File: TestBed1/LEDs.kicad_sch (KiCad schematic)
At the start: 6 parts, among them U3 TLC5973

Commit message: WIP - Parts Assigned
Need footprints, and MCU connections, but WIP
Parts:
- removed D1, D2, D3: D, symbol Device:D
- added C10, C8: 0.1u, symbol Device:C
- added C11: C, symbol Device:C
- added D1, D2, D3: LED, LED_SMD:LED_1206_3216Metric, symbol Device:LED
- added R5: 0, symbol Device:R
- added U6: TXB0101DBV, Package_TO_SOT_SMD:SOT-23-6, symbol Logic_LevelTranslator:TXB0101DBV
- added U7: ~, symbol New_Library:SFH_5711-2/3-Z
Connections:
- net +3V3: now also C11.1, C8.1, R5.1, U6.1 (V_{CCA}), U7.3 (VCC); no longer C2.1, U3.8 (VCC)
- net D1: now also D1.1 (K), D2.1 (K), D3.1 (K)
- net GND: now also C10.2, C11.2, C8.2, U6.2 (GND), U7.1 (GND), U7.2 (GND)
- net LED_IN: now also U6.3 (A); no longer U3.6 (SDI)
- new net: R5.2, U6.5 (OE)
- new net +5V: C10.1, C2.1, D1.2 (A), D2.2 (A), D3.2 (A), U3.8 (VCC), U6.6 (V_{CCB})
- new net AMB_OUT: U7.4 (OUT)
- new net LED_OUT: U3.6 (SDI), U6.4 (B)
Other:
- note added: "TODO BH1620FVC-TR Ambient"
- note removed: "TODO BH1620FVC"

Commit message: LED Update for more work
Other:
- note added: "TODO Heartbeat LED"
- note added: "TODO MCU crashed LED"
- note added: "TODO maybe intend to extend further with more of above LED drivers?"
- note added: "TODO reserve castelated area?"
- note added: "TODO reverse mounted warning indicators."
- note added: "TODO swap whites for reds"
- moved on the sheet: C11, U7
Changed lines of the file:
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@@
 	(paper "A4")
 	(junction
-		(at 121.92 149.86)
+		(at 146.05 175.26)
 		(diameter 0)
 		(color 0 0 0 0)
@@
 	(wire
 		(pts
-			(xy 123.19 149.86) (xy 123.19 148.59)
+			(xy 147.32 175.26) (xy 147.32 173.99)
 		)
 		(stroke
@@
 	(wire
 		(pts
-			(xy 121.92 151.13) (xy 121.92 149.86)
+			(xy 146.05 176.53) (xy 146.05 175.26)
 		)
 		(stroke
@@
 	(wire
 		(pts
-			(xy 121.92 149.86) (xy 120.65 149.86)
+			(xy 146.05 175.26) (xy 144.78 175.26)
 		)
 		(stroke
@@
 	(wire
 		(pts
-			(xy 121.92 149.86) (xy 123.19 149.86)
+			(xy 146.05 175.26) (xy 147.32 175.26)
 		)
 		(stroke
@@
 	(wire
 		(pts
-			(xy 120.65 149.86) (xy 120.65 148.59)
+			(xy 144.78 175.26) (xy 144.78 173.99)
 		)
 		(stroke
@@
 		)
 	)
+	(text "TODO swap whites for reds"
+		(exclude_from_sim no)
+		(at 110.744 89.408 0)
+		(effects
+			(font
+				(size 1.27 1.27)
+			)
+		)
+	)
+	(text "TODO maybe intend to extend further with more of above LED drivers?"
+		(exclude_from_sim no)
+		(at 143.764 115.824 0)
+		(effects
+			(font
+				(size 1.27 1.27)
+			)
+		)
+	)
 	(text "5k ~= 10mA as max Current"
 		(exclude_from_sim no)
 		(at 119.634 80.518 0)
+		(effects
+			(font
+				(size 1.27 1.27)
+			)
+		)
+	)
+	(text "TODO reverse mounted warning indicators."
+		(exclude_from_sim no)
+		(at 139.7 105.918 0)
+		(effects
+			(font
+				(size 1.27 1.27)
+			)
+		)
+	)
+	(text "TODO MCU crashed LED"
+		(exclude_from_sim no)
+		(at 130.302 101.854 0)
+		(effects
+			(font
+				(size 1.27 1.27)
+			)
+		)
+	)
+	(text "TODO Heartbeat LED"
+		(exclude_from_sim no)
+		(at 127 97.028 0)
+		(effects
+			(font
+				(size 1.27 1.27)
+			)
+		)
+	)
+	(text "TODO reserve castelated area?"
+		(exclude_from_sim no)
+		(at 133.604 110.236 0)
 		(effects
 			(font
@@
 	)
 	(label "AMB_OUT"
-		(at 125.73 137.16 0)
+		(at 149.86 162.56 0)
 		(effects
 			(font
@@
 	(symbol
 		(lib_id "power:GND")
-		(at 106.68 148.59 0)
+		(at 130.81 173.99 0)
 		(unit 1)
 		(exclude_from_sim no)
@@
 		(fields_autoplaced yes)
 		(property "Reference" "#PWR043"
-			(at 106.68 154.94 0)
+			(at 130.81 180.34 0)
 			(effects
 				(font
@@
 		)
 		(property "Value" "GND"
-			(at 106.68 153.67 0)
-			(effects
-				(font
-					(size 1.27 1.27)
-				)
-			)
-		)
-		(property "Footprint" ""
-			(at 106.68 148.59 0)
+			(at 130.81 179.07 0)
+			(effects
+				(font
+					(size 1.27 1.27)
+				)
+			)
+		)
+		(property "Footprint" ""
+			(at 130.81 173.99 0)
 			(effects
 				(font
@@
 		)
 		(property "Datasheet" ""
-			(at 106.68 148.59 0)
+			(at 130.81 173.99 0)
 			(effects
 				(font
@@
 		)
 		(property "Description" "Power symbol creates a global label with name \"GND\" , ground"
-			(at 106.68 148.59 0)
+			(at 130.81 173.99 0)
 			(effects
 				(font
@@
 	(symbol
 		(lib_id "New_Library:SFH_5711-2/3-Z")
-		(at 123.19 140.97 0)
+		(at 147.32 166.37 0)
 		(unit 1)
 		(exclude_from_sim no)
@@
 		(fields_autoplaced yes)
 		(property "Reference" "U7"
-			(at 128.27 142.2399 0)
+			(at 152.4 167.6399 0)
 			(effects
 				(font
@@
 		)
 		(property "Value" "~"
-			(at 128.27 144.145 0)
+			(at 152.4 169.545 0)
 			(effects
 				(font
@@
 		)
 		(property "Footprint" ""
-			(at 123.19 140.97 0)
+			(at 147.32 166.37 0)
 			(effects
 				(font
@@
 		)
 		(property "Datasheet" ""
-			(at 123.19 140.97 0)
+			(at 147.32 166.37 0)
 			(effects
 				(font
@@
 		)
 		(property "Description" ""
-			(at 123.19 140.97 0)
+			(at 147.32 166.37 0)
 			(effects
 				(font
@@
 	(symbol
 		(lib_id "power:GND")
-		(at 121.92 151.13 0)
+		(at 146.05 176.53 0)
 		(unit 1)
 		(exclude_from_sim no)
@@
 		(fields_autoplaced yes)
 		(property "Reference" "#PWR042"
-			(at 121.92 157.48 0)
+			(at 146.05 182.88 0)
 			(effects
 				(font
@@
 		)
 		(property "Value" "GND"
-			(at 121.92 156.21 0)
-			(effects
-				(font
-					(size 1.27 1.27)
-				)
-			)
-		)
-		(property "Footprint" ""
-			(at 121.92 151.13 0)
+			(at 146.05 181.61 0)
+			(effects
+				(font
+					(size 1.27 1.27)
+				)
+			)
+		)
+		(property "Footprint" ""
+			(at 146.05 176.53 0)
 			(effects
 				(font
@@
 		)
 		(property "Datasheet" ""
-			(at 121.92 151.13 0)
+			(at 146.05 176.53 0)
 			(effects
 				(font
@@
 		)
 		(property "Description" "Power symbol creates a global label with name \"GND\" , ground"
-			(at 121.92 151.13 0)
+			(at 146.05 176.53 0)
 			(effects
 				(font
@@
 	(symbol
 		(lib_id "power:+3V3")
-		(at 118.11 137.16 0)
+		(at 142.24 162.56 0)
 		(unit 1)
 		(exclude_from_sim no)
@@
 		(fields_autoplaced yes)
 		(property "Reference" "#PWR040"
-			(at 118.11 140.97 0)
+			(at 142.24 166.37 0)
 			(effects
 				(font
@@
 		)
 		(property "Value" "+3V3"
-			(at 118.11 132.08 0)
-			(effects
-				(font
-					(size 1.27 1.27)
-				)
-			)
-		)
-		(property "Footprint" ""
-			(at 118.11 137.16 0)
+			(at 142.24 157.48 0)
+			(effects
+				(font
+					(size 1.27 1.27)
+				)
+			)
+		)
+		(property "Footprint" ""
+			(at 142.24 162.56 0)
 			(effects
 				(font
@@
 		)
 		(property "Datasheet" ""
-			(at 118.11 137.16 0)
+			(at 142.24 162.56 0)
 			(effects
 				(font
@@
 		)
 		(property "Description" "Power symbol creates a global label with name \"+3V3\""
-			(at 118.11 137.16 0)
+			(at 142.24 162.56 0)
 			(effects
 				(font
@@
 	(symbol
 		(lib_id "Device:C")
-		(at 106.68 144.78 0)
+		(at 130.81 170.18 0)
 		(unit 1)
 		(exclude_from_sim no)
@@
 		(fields_autoplaced yes)
 		(property "Reference" "C11"
-			(at 110.49 143.5099 0)
+			(at 134.62 168.9099 0)
 			(effects
 				(font
@@
 		)
 		(property "Value" "C"
-			(at 110.49 146.0499 0)
+			(at 134.62 171.4499 0)
 			(effects
 				(font
@@
 		)
 		(property "Footprint" ""
-			(at 107.6452 148.59 0)
+			(at 131.7752 173.99 0)
 			(effects
 				(font
@@
 		)
 		(property "Datasheet" "~"
-			(at 106.68 144.78 0)
+			(at 130.81 170.18 0)
 			(effects
 				(font
@@
 		)
 		(property "Description" "Unpolarized capacitor"
-			(at 106.68 144.78 0)
+			(at 130.81 170.18 0)
 			(effects
 				(font
@@
 	(symbol
 		(lib_id "power:+3V3")
-		(at 106.68 140.97 0)
+		(at 130.81 166.37 0)
 		(unit 1)
 		(exclude_from_sim no)
@@
 		(fields_autoplaced yes)
 		(property "Reference" "#PWR041"
-			(at 106.68 144.78 0)
+			(at 130.81 170.18 0)
 			(effects
 				(font
@@
 		)
 		(property "Value" "+3V3"
-			(at 106.68 135.89 0)
-			(effects
-				(font
-					(size 1.27 1.27)
-				)
-			)
-		)
-		(property "Footprint" ""
-			(at 106.68 140.97 0)
+			(at 130.81 161.29 0)
+			(effects
+				(font
+					(size 1.27 1.27)
+				)
+			)
+		)
+		(property "Footprint" ""
+			(at 130.81 166.37 0)
 			(effects
 				(font
@@
 		)
 		(property "Datasheet" ""
-			(at 106.68 140.97 0)
+			(at 130.81 166.37 0)
 			(effects
 				(font
@@
 		)
 		(property "Description" "Power symbol creates a global label with name \"+3V3\""
-			(at 106.68 140.97 0)
-			(effects
-				(font
+			(at 130.81 166.37 0)
+			(effects
+				(font

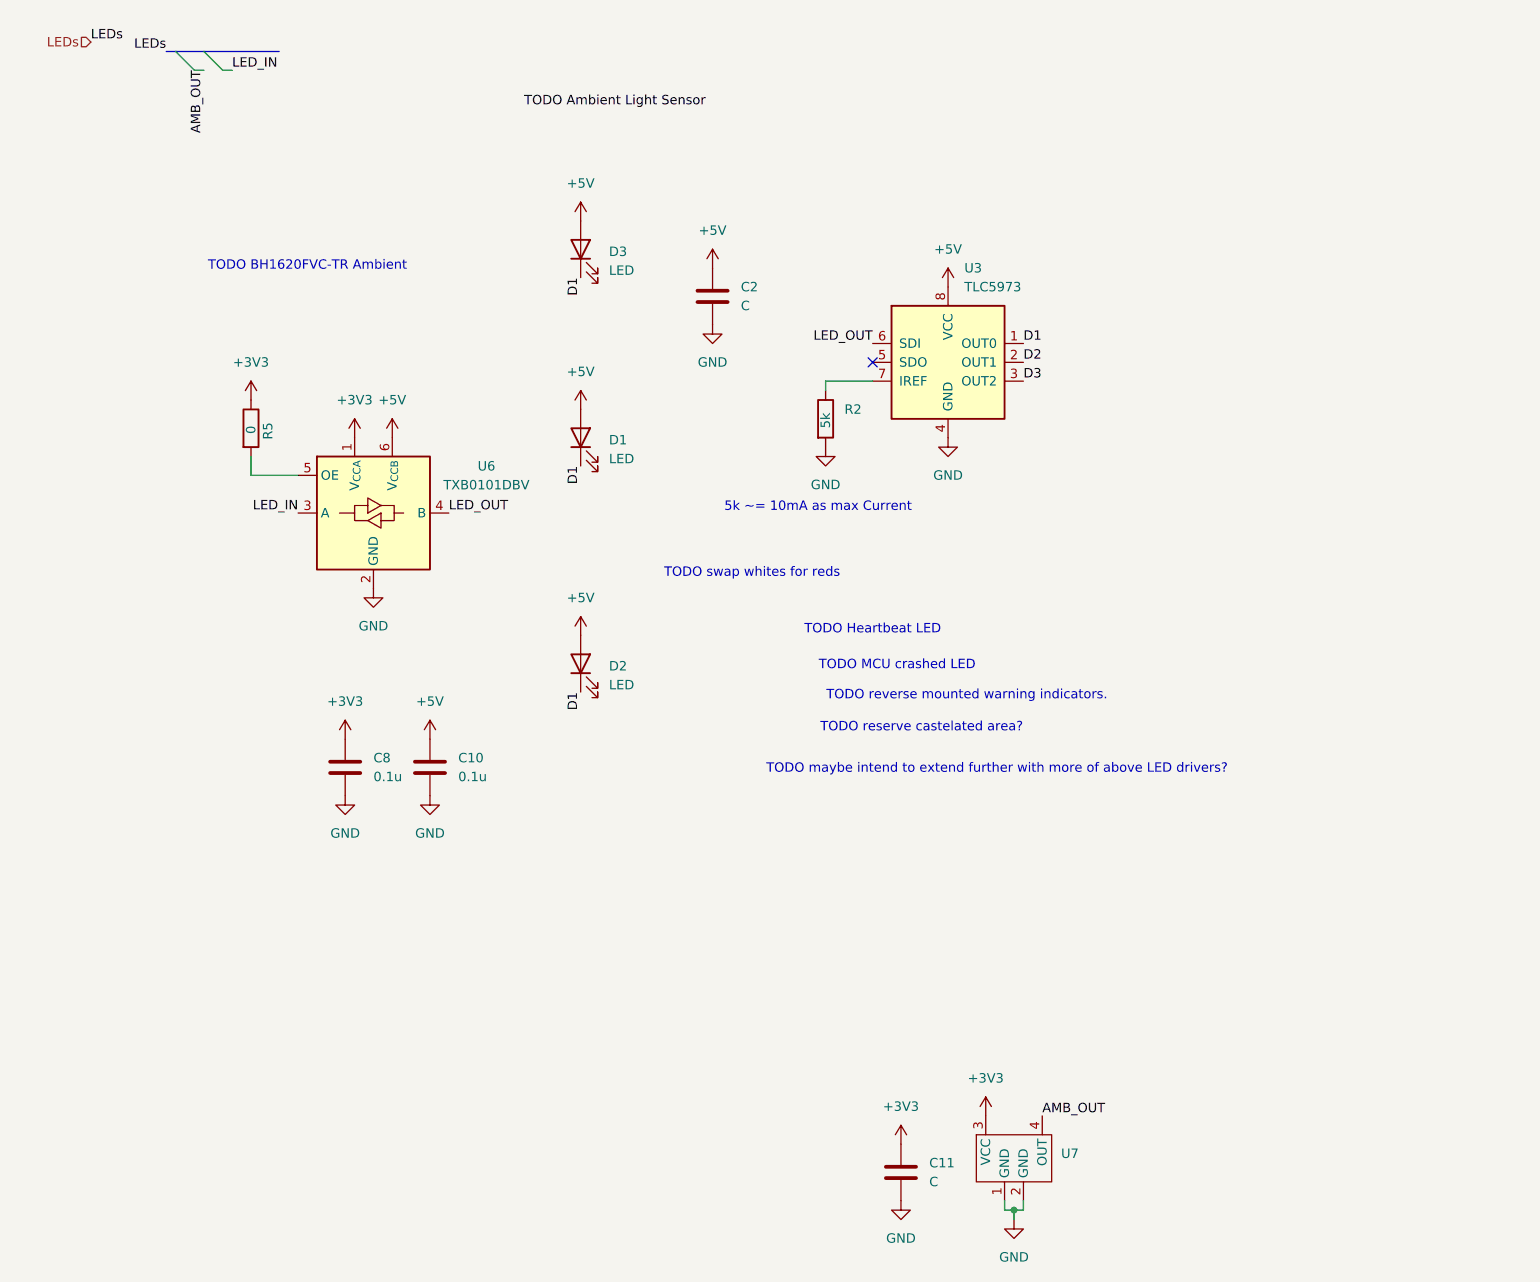
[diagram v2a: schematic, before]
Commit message: Rough Grouping, Passive Footprint Assignment
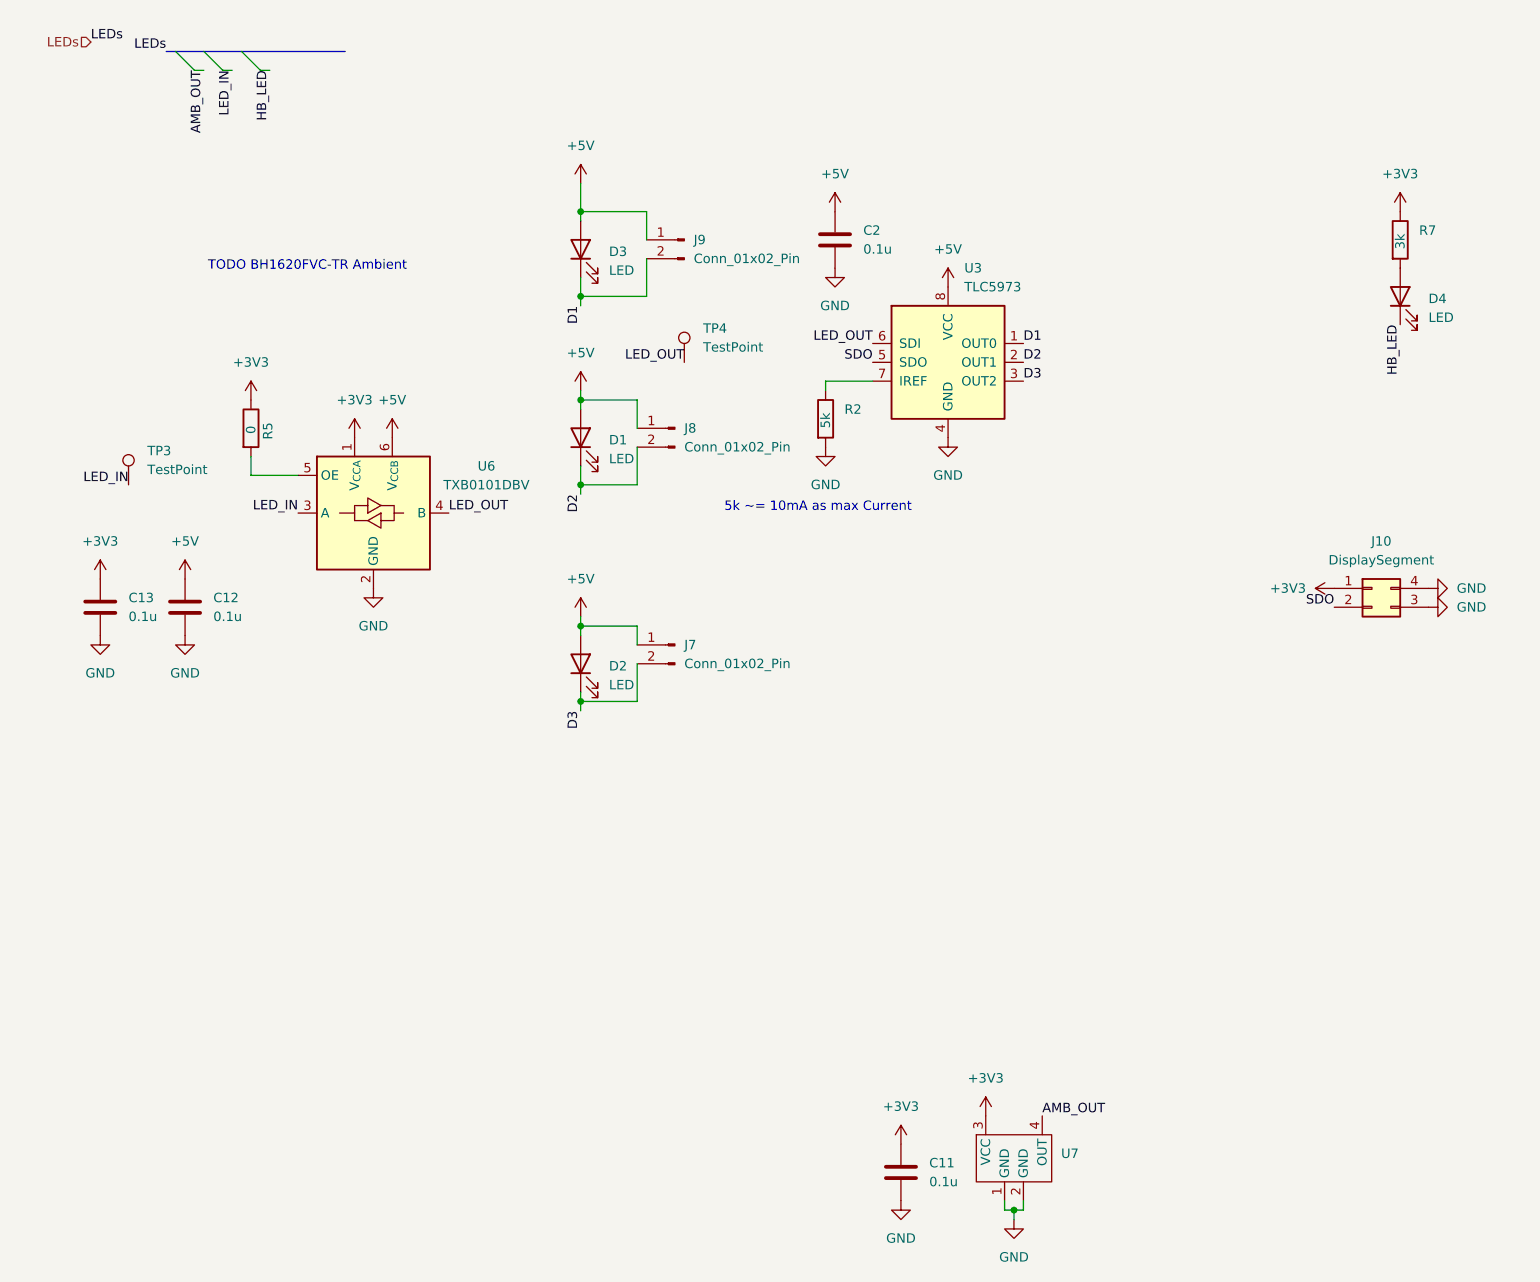
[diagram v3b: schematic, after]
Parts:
- removed C10, C8: 0.1u, symbol Device:C
- added C12, C13: 0.1u, Capacitor_SMD:C_0402_1005Metric_Pad0.74x0.62mm_HandSolder, symbol Device:C
- added D4: LED, LED_SMD:LED_0603_1608Metric, symbol Device:LED
- added J10: DisplaySegment, Library:DisplayPassthrough, symbol Connector_Generic:Conn_02x02_Counter_Clockwise
- added J7, J8, J9: Conn_01x02_Pin, Connector_PinHeader_2.54mm:PinHeader_1x02_P2.54mm_Vertical, symbol Connector:Conn_01x02_Pin
- added R7: 3k, Resistor_SMD:R_0603_1608Metric, symbol Device:R
- added TP3, TP4: TestPoint, TestPoint:TestPoint_Pad_1.0x1.0mm, symbol Connector:TestPoint
- C11, C2: value C -> 0.1u; footprint (none) -> Capacitor_SMD:C_0402_1005Metric_Pad0.74x0.62mm_HandSolder
- D1, D2, D3: footprint LED_SMD:LED_1206_3216Metric -> LED_SMD:LED_Luminus_MP-3030-1100_3.0x3.0mm
- R2, R5: footprint (none) -> Resistor_SMD:R_0402_1005Metric
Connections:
- net +3V3: now also C13.1, J10.1 (Pin_1), R7.1
- net +5V: now also C12.1, J7.1 (Pin_1), J8.1 (Pin_1), J9.1 (Pin_1)
- net D1: now also J9.2 (Pin_2); no longer D1.1 (K), D2.1 (K)
- net D2: now also D1.1 (K), J8.2 (Pin_2)
- net D3: now also D2.1 (K), J7.2 (Pin_2)
- net GND: now also C12.2, C13.2, J10.3 (Pin_3), J10.4 (Pin_4)
- net LED_IN: now also TP3.1
- net LED_OUT: now also TP4.1
- net SDO: now reaches U3.5 (SDO)
- net SDO: now also J10.2 (Pin_2)
- new net: D4.2 (A), R7.2
- new net HB_LED: D4.1 (K)
- no-connect marks 1 -> 0
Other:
- note removed: "TODO Heartbeat LED"
- note removed: "TODO MCU crashed LED"
- note removed: "TODO maybe intend to extend further with more of above LED drivers?"
- note removed: "TODO reserve castelated area?"
- note removed: "TODO reverse mounted warning indicators."
- note removed: "TODO swap whites for reds"
- moved on the sheet: C2

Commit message: Schematic Assignment, board assignemtn and rough placement
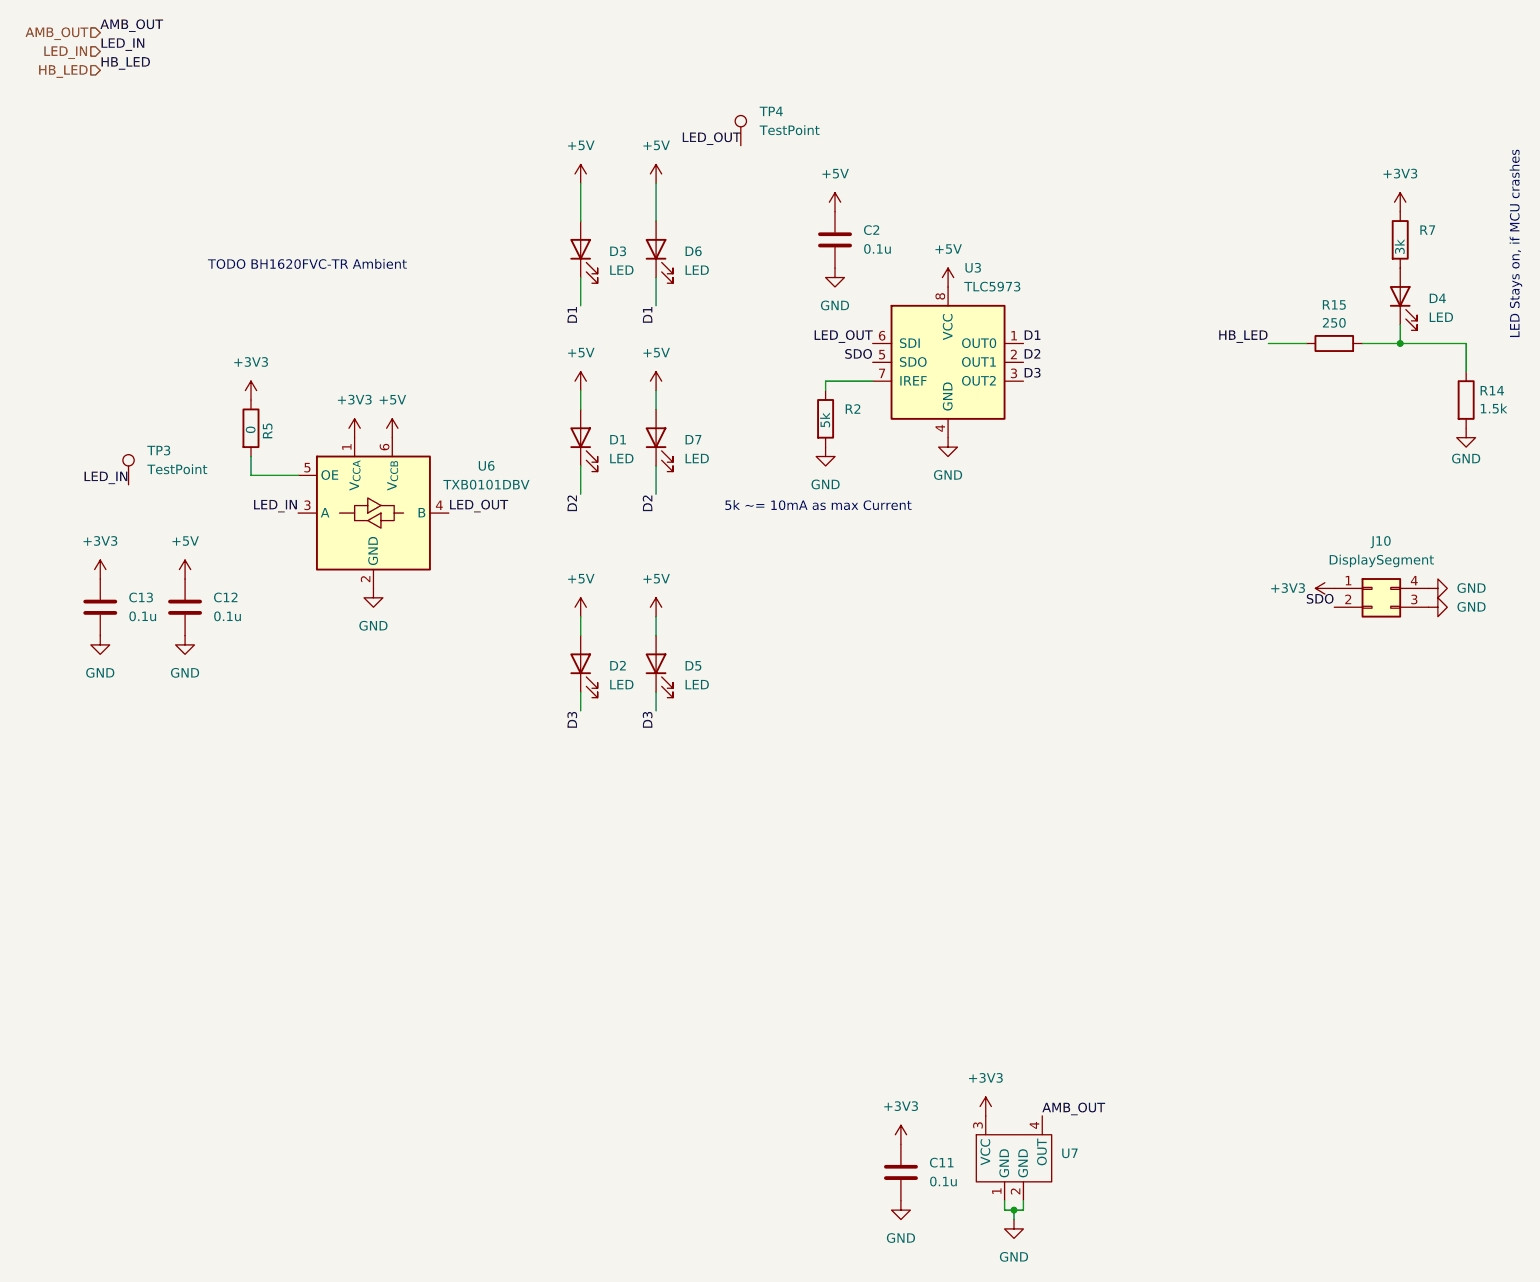
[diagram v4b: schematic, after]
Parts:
- removed J7, J8, J9: Conn_01x02_Pin, Connector_PinHeader_2.54mm:PinHeader_1x02_P2.54mm_Vertical, symbol Connector:Conn_01x02_Pin
- added D5, D6, D7: LED, LED_SMD:LED_Luminus_MP-3030-1100_3.0x3.0mm, symbol Device:LED
- added R14: 1.5k, Resistor_SMD:R_0402_1005Metric, symbol Device:R
- added R15: 250, Resistor_SMD:R_0402_1005Metric, symbol Device:R
- J10: footprint Library:DisplayPassthrough -> X27:DisplayPassthrough
- U7: footprint (none) -> X27:SFH_5711-23-Z
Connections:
- net +5V: now also D5.2 (A), D6.2 (A), D7.2 (A)
- net D1: now also D6.1 (K)
- net D2: now also D7.1 (K)
- net D3: now also D5.1 (K)
- net GND: now also R14.2
- net HB_LED: now also R15.1; no longer D4.1 (K)
- new net: D4.1 (K), R14.1, R15.2
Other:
- note added: "LED Stays on, if MCU crashes"
- moved on the sheet: TP4
